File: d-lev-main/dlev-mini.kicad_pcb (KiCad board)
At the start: 4 copper layers, 175.3 x 163.3 mm, 126 parts, among them J1 Conn_01x12_MountingPin, J2 Tag-Connect TC2030-NL, J3 S8B-PH-SM4-TB, J4 S8B-PH-SM4-TB, J5 Conn_01x06_MountingPin, Q1 BSS138, Q2 BSS138, Q3 BSS138, Q4 BSS138, Q5 BSS138, SW1 RotaryEncoder_Switch, SW2 RotaryEncoder_Switch, SW3 RotaryEncoder_Switch, SW4 RotaryEncoder_Switch, SW5 RotaryEncoder_Switch, SW6 RotaryEncoder_Switch, SW7 RotaryEncoder_Switch, SW8 RotaryEncoder_Switch, U1 25LCxxx, U2 AMS1117-3.3, U3 AC608

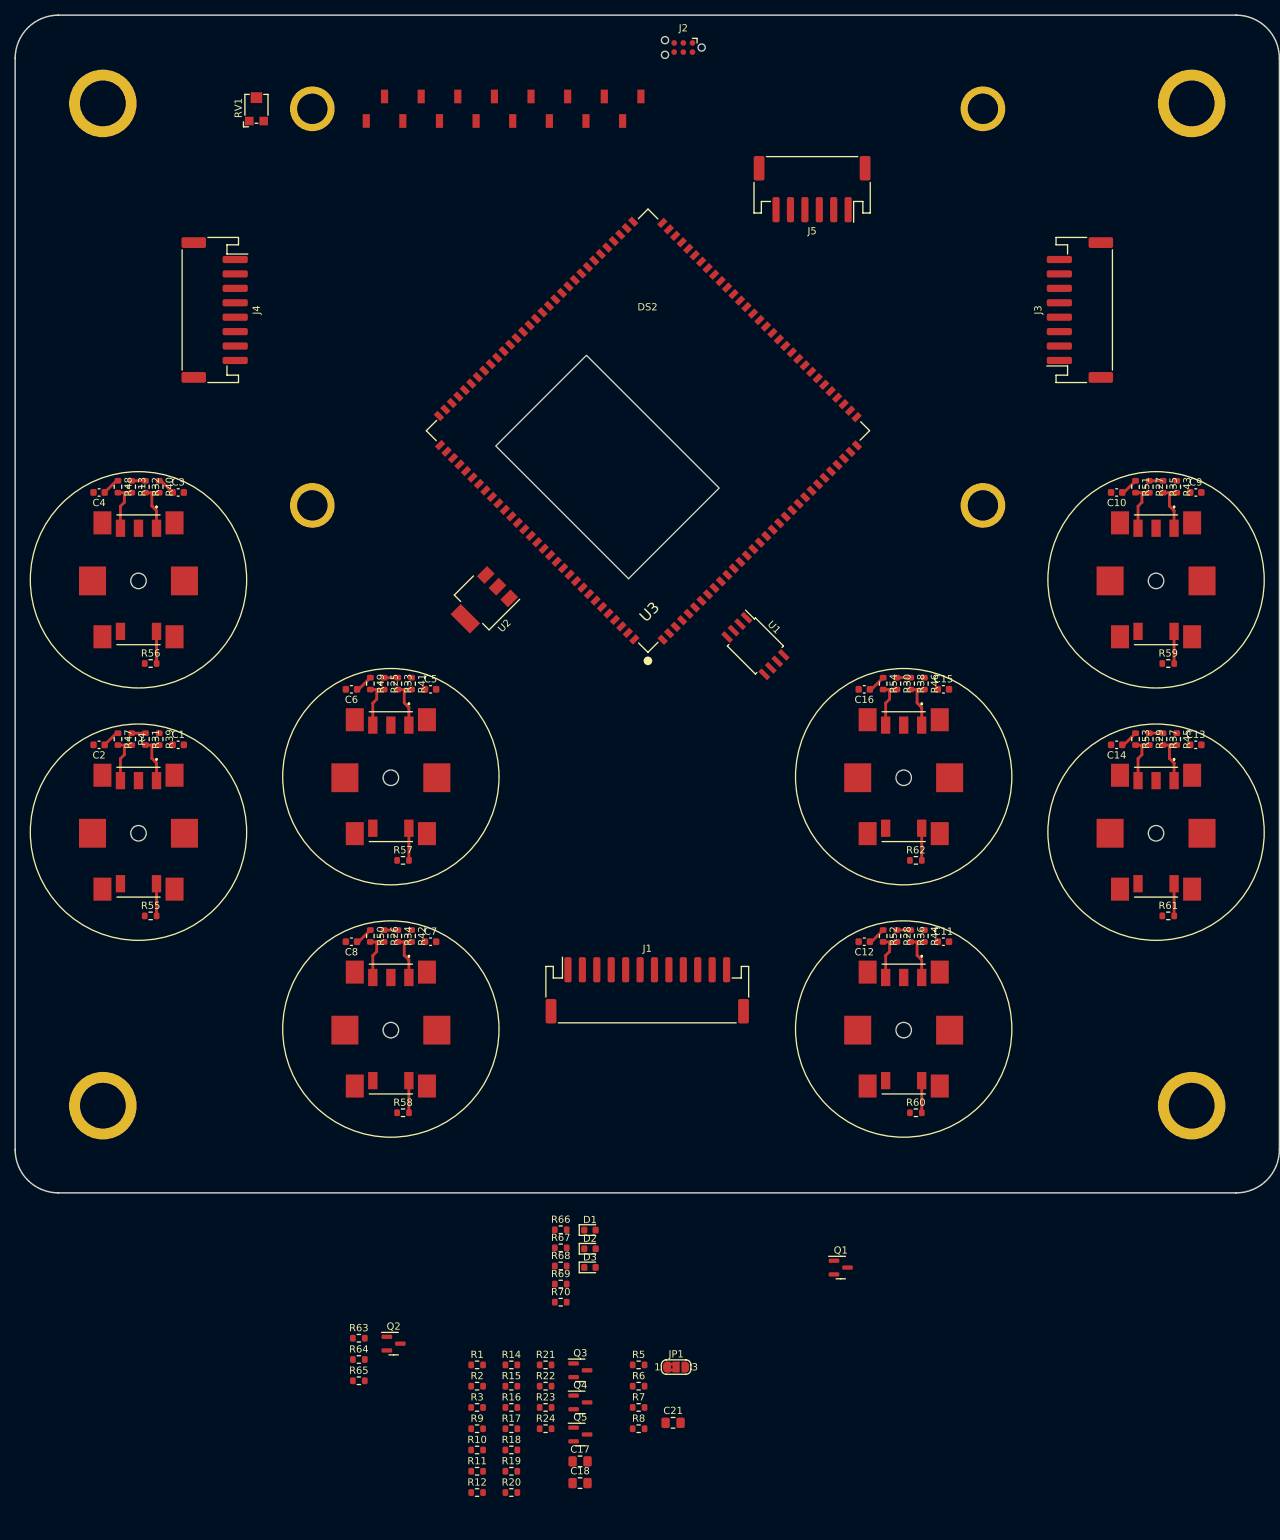
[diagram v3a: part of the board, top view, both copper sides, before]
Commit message: mostly done routing
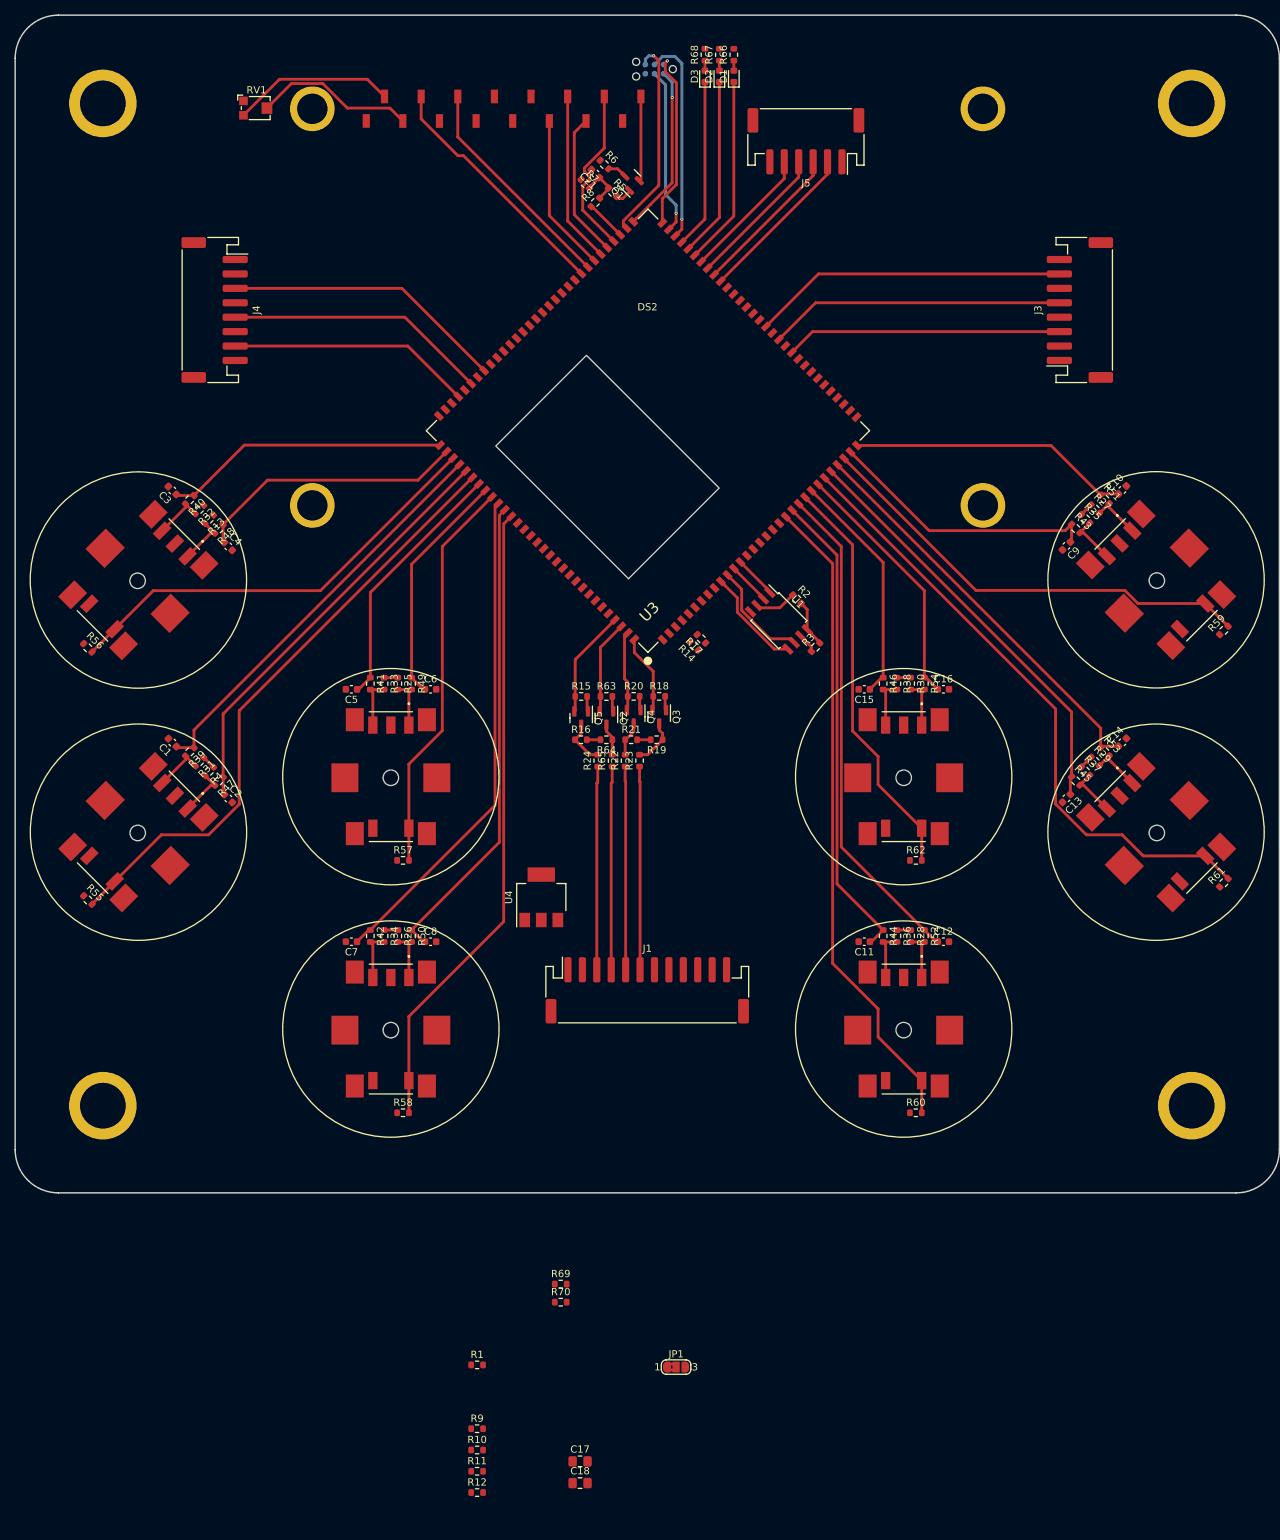
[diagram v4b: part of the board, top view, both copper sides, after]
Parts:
- removed U2: AMS1117-3.3, Package_TO_SOT_SMD:SOT-223-3_TabPin2
- added U4: AMS1117-3.3, Package_TO_SOT_SMD:SOT-223-3_TabPin2, F.Cu at (-14.7, 11.8)
- C21: footprint Capacitor_SMD:C_0805_2012Metric_Pad1.18x1.45mm_HandSolder -> Capacitor_SMD:C_0603_1608Metric
- J1: value Conn_01x12_MountingPin -> S12B-PH-SM4-TB
- J2: moved to B.Cu
- J5: value Conn_01x06_MountingPin -> S6B-PH-SM4-TB
- R24, R65: value 220 -> 1k
- moved C21 173.6 mm to (-7.20, -88.5), turned to 135 degrees
- moved R8 170.2 mm to (-7.20, -84.5), turned to 45 degrees
- moved R7 169.9 mm to (-8.60, -87.1), turned to -45 degrees
- moved R6 169.5 mm to (-5.95, -89.8), turned to -45 degrees
- moved R68 169.2 mm to (8.00, -105.0), turned to 90 degrees
- moved R67 166.9 mm to (10.0, -105.0), turned to 90 degrees
- moved D3 165.9 mm to (8.00, -102.0), turned to 90 degrees
- moved R66 164.7 mm to (12.0, -105.0), turned to 90 degrees
- moved D2 163.6 mm to (10.0, -102.0), turned to 90 degrees
- moved R5 162.7 mm to (-4.80, -85.9), turned to -45 degrees
- moved D1 161.2 mm to (12.0, -102.0), turned to 90 degrees
- moved Q1 153.5 mm to (-2.45, -87.5), turned to 135 degrees
- moved R2 117.8 mm to (20.8, -29.5), turned to -45 degrees
- moved R3 115.4 mm to (23.3, -22.8), turned to 45 degrees
- moved R17 112.7 mm to (7.50, -24.0), turned to 135 degrees
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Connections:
- net midi_out_lo renamed midi_out
- J5 pad 1: /FPGA/tuner.oe -> GND
- J5 pad 2: /FPGA/tuner.le -> /FPGA/tuner.oe
- J5 pad 3: /FPGA/tuner.sda -> /FPGA/tuner.le
- J5 pad 4: /FPGA/tuner.scl -> /FPGA/tuner.sda
- J5 pad 5: GND -> /FPGA/tuner.scl
- Q2 pad 2: /midi_rx_n -> /midi_rx
- Q5 pad 2: /midi_tx_n -> /midi_tx
- R15 pad 1: /midi_tx_n -> /midi_tx
- R63 pad 1: /midi_rx_n -> /midi_rx
- U3 pad 100: /FPGA/enc_3.a -> /FPGA/enc_3.b
- U3 pad 101: /FPGA/enc_3.b -> /FPGA/enc_3.a
- U3 pad 103: /FPGA/enc_4.a -> /FPGA/enc_4.b
- U3 pad 104: /FPGA/enc_4.b -> /FPGA/enc_4.a
- U3 pad 112: unconnected-(U3-I_R8-Pad112) -> GND
- U3 pad 113: unconnected-(U3-I_T8-Pad113) -> GND
- U3 pad 114: unconnected-(U3-I_R9-Pad114) -> GND
- U3 pad 115: unconnected-(U3-I_T9-Pad115) -> GND
- U3 pad 121: /FPGA/midi_tx -> /midi_tx
- U3 pad 122: /FPGA/midi_rx -> /midi_rx
- U3 pad 43: unconnected-(U3-I_B9-Pad43) -> GND
- U3 pad 45: unconnected-(U3-I_A8-Pad45) -> GND
- U3 pad 47: unconnected-(U3-I_B8-Pad47) -> GND
- U3 pad 65: /FPGA/lcd_pwm -> /FPGA/lcd.pwm
- U3 pad 87: unconnected-(U3-LVDS_TX1_P-Pad87) -> GND
- U3 pad 89: unconnected-(U3-LVDS_TX2_P-Pad89) -> GND
- U3 pad 91: unconnected-(U3-LVDS_TX3_P-Pad91) -> GND
- U3 pad 94: /FPGA/enc_1.a -> /FPGA/enc_1.b
- U3 pad 95: /FPGA/enc_1.b -> /FPGA/enc_1.a
- U3 pad 97: /FPGA/enc_2.a -> /FPGA/enc_2.b
- U3 pad 98: /FPGA/enc_2.b -> /FPGA/enc_2.a
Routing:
- net /FPGA/enc_8.s: track 4.47 -> 90.5 mm
- net /FPGA/enc_4.s: track 4.47 -> 88.6 mm
- net /FPGA/enc_6.s: track 4.47 -> 86.7 mm
- net /FPGA/enc_2.s: track 4.47 -> 84.9 mm
- net /FPGA/enc_4.b: track 0.00 -> 69.0 mm
- net /FPGA/enc_8.a: track 2.51 -> 68.9 mm
- net /FPGA/enc_8.b: track 0.00 -> 66.0 mm
- net /FPGA/enc_4.a: track 2.51 -> 66.2 mm
- net /FPGA/enc_6.b: track 0.00 -> 58.7 mm
- net /FPGA/enc_5.s: track 4.47 -> 62.9 mm
- net /FPGA/enc_2.b: track 0.00 -> 57.0 mm
- net /FPGA/enc_1.s: track 4.47 -> 61.2 mm
- net /FPGA/enc_2.a: track 2.51 -> 58.9 mm
- net /FPGA/enc_6.a: track 2.51 -> 56.9 mm
- net /FPGA/enc_7.s: track 4.47 -> 57.1 mm
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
